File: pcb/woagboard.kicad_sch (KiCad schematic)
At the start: 94 parts, among them J1 Battery JST, J2 Flash connection, J3 Battery JST, J4 Flash connection, SW10 SW_Push, SW11 SW_Push, SW12 SW_Push, SW13 SW_Push, SW14 SW_Push, SW15 SW_Push, SW16 SW_Push, SW17 SW_Push, SW18 SW_Push, SW19 SW_Push, SW20 SW_Push, SW21 SW_Push, SW22 SW_Push, SW23 SW_Push, SW24 SW_Push, SW25 SW_Push, SW26 SW_Push, SW27 SW_Push, SW28 SW_Push, SW29 SW_Push, SW3 SW_Push, SW30 SW_Push, SW31 SW_Push, SW32 SW_Push, SW33 SW_Push, SW34 SW_Push, SW35 SW_Push, SW36 SW_Push, SW4 SW_Push, SW5 SW_Push, SW6 SW_Push, SW7 SW_Push, SW8 SW_Push, SW9 SW_Push, U1 USBLC6-2, U2 USBLC6-2, U3 BQ24075, U4 BQ24075, U5 nRF52840_E73-2G4M08S1C, U9 nRF52840_E73-2G4M08S1C, Y1 32.768 KHz, Y2 32.768 KHz

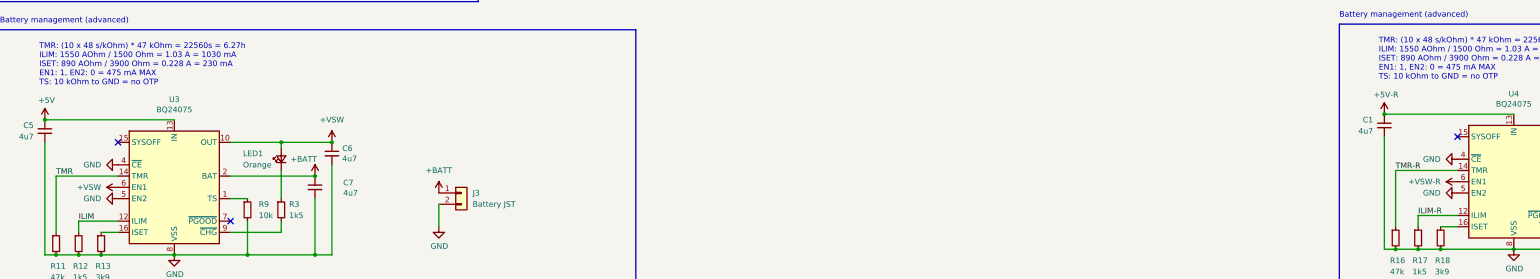
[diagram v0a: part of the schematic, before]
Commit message: fix: fix the single biggest mistake on the board
I blew up the left half because of this missing trace. No idea how to fix my current boards now....
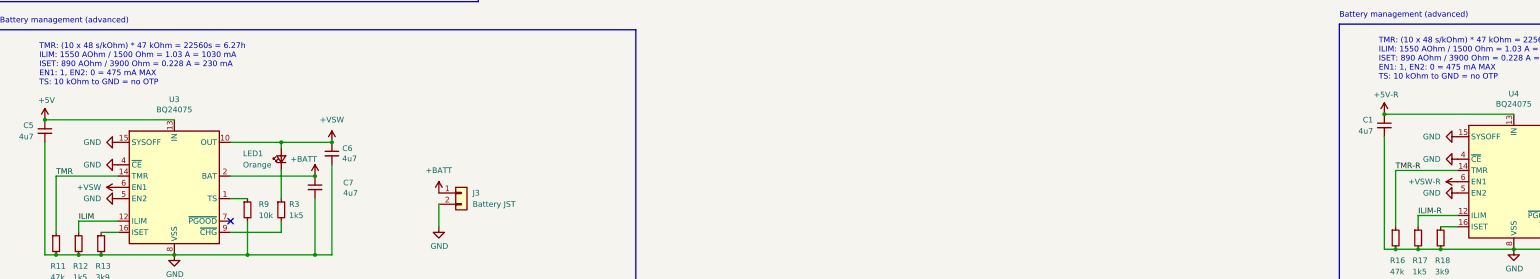
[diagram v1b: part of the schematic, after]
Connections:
- net GND: now also U3.15 (SYSOFF), U4.15 (SYSOFF)
- no-connect marks 28 -> 26
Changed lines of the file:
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@@
 	)
 	(no_connect
-		(at 44.45 116.84)
-	)
-	(no_connect
 		(at 415.29 233.68)
 	)
@@
 	)
 	(no_connect
-		(at 346.71 115.57)
-	)
-	(no_connect
 		(at 415.29 236.22)
 	)
@@
 	)
 	(symbol
+		(lib_id "power:GND")
+		(at 44.45 116.84 270)
+		(unit 1)
+		(exclude_from_sim no)
+		(in_bom yes)
+		(on_board yes)
+		(dnp no)
+		(fields_autoplaced yes)
+		(property "Reference" "#PWR050"
+			(at 38.1 116.84 0)
+			(effects
+				(font
+					(size 1.27 1.27)
+				)
+				(hide yes)
+			)
+		)
+		(property "Value" "GND"
+			(at 40.64 116.8399 90)
+			(effects
+				(font
+					(size 1.27 1.27)
+				)
+				(justify right)
+			)
+		)
+		(property "Footprint" ""
+			(at 44.45 116.84 0)
+			(effects
+				(font
+					(size 1.27 1.27)
+				)
+				(hide yes)
+			)
+		)
+		(property "Datasheet" ""
+			(at 44.45 116.84 0)
+			(effects
+				(font
+					(size 1.27 1.27)
+				)
+				(hide yes)
+			)
+		)
+		(property "Description" "Power symbol creates a global label with name \"GND\" , ground"
+			(at 44.45 116.84 0)
+			(effects
+				(font
+					(size 1.27 1.27)
+				)
+				(hide yes)
+			)
+		)
+		(pin "1"
+		)
+		(instances
+			(project "woagboard"
+				(path "/c2a65ddb-3915-4293-98a9-444287fe2a3d"
+					(reference "#PWR050")
+					(unit 1)
+				)
+			)
+		)
+	)
+	(symbol
 		(lib_id "Device:C_Small")
 		(at 148.59 182.88 0)
@@
 					(unit 1)
 				)
+			)
+		)
+	)
+	(symbol
+		(lib_id "power:GND")
+		(at 346.71 115.57 270)
+		(unit 1)
+		(exclude_from_sim no)
+		(in_bom yes)
+		(on_board yes)
+		(dnp no)
+		(fields_autoplaced yes)
+		(property "Reference" "#PWR055"
+			(at 340.36 115.57 0)
+			(effects
+				(font
+					(size 1.27 1.27)
+				)
+				(hide yes)
+			)
+		)
+		(property "Value" "GND"
+			(at 342.9 115.5699 90)
+			(effects
+				(font
+					(size 1.27 1.27)
+				)
+				(justify right)
+			)
+		)
+		(property "Footprint" ""
+			(at 346.71 115.57 0)
+			(effects
+				(font
+					(size 1.27 1.27)
+				)
+				(hide yes)
+			)
+		)
+		(property "Datasheet" ""
+			(at 346.71 115.57 0)
+			(effects
+				(font
+					(size 1.27 1.27)
+				)
+				(hide yes)
+			)
+		)
+		(property "Description" "Power symbol creates a global label with name \"GND\" , ground"
+			(at 346.71 115.57 0)
+			(effects
+				(font
+					(size 1.27 1.27)
+				)
+				(hide yes)
+			)
+		)
+		(pin "1"
+		)
+		(instances
+			(project "woagboard"
+				(path "/c2a65ddb-3915-4293-98a9-444287fe2a3d"
+					(reference "#PWR055")
+					(unit 1)
+				)
